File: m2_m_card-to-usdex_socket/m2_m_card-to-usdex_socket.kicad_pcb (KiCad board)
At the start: 6 copper layers, 22 x 80 mm, 11 parts, among them J1 Bus_M.2_Socket_M, J2 Micro_SDex_Card_Det1, U1 AMS1117-1.8

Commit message: m2_m_card-to-usdex_socket: Add impedance information
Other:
- board text added: "Impedance controlled for: JLC06081H-2116 Layers: 6 PCB Thickness: 0.8mm Inner Copper Weight: 0.5oz Outer Copper Weight: 1oz Impedance: 85Ω Type: Differential Pair (Non coplanar) Signal Layer: L1 Top Ref: / Bottom Ref: L2 Trace Spacing: 8 mil Trace Width: 8.0800 mil"
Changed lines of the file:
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@@
+		)
+	)
+	(gr_text "Impedance controlled for: JLC06081H-2116\n\nLayers: 6\nPCB Thickness: 0.8mm\nInner Copper Weight: 0.5oz\nOuter Copper Weight: 1oz\nImpedance: 85Ω\nType: Differential Pair (Non coplanar)\nSignal Layer: L1\nTop Ref: /\nBottom Ref: L2\nTrace Spacing: 8 mil\nTrace Width: 8.0800 mil"
+		(at 220.4 79 0)
+		(layer "Cmts.User")
+		(effects
+			(font
+				(size 1 1)
+				(thickness 0.15)
+			)
+			(justify left bottom)
 		)
 	)

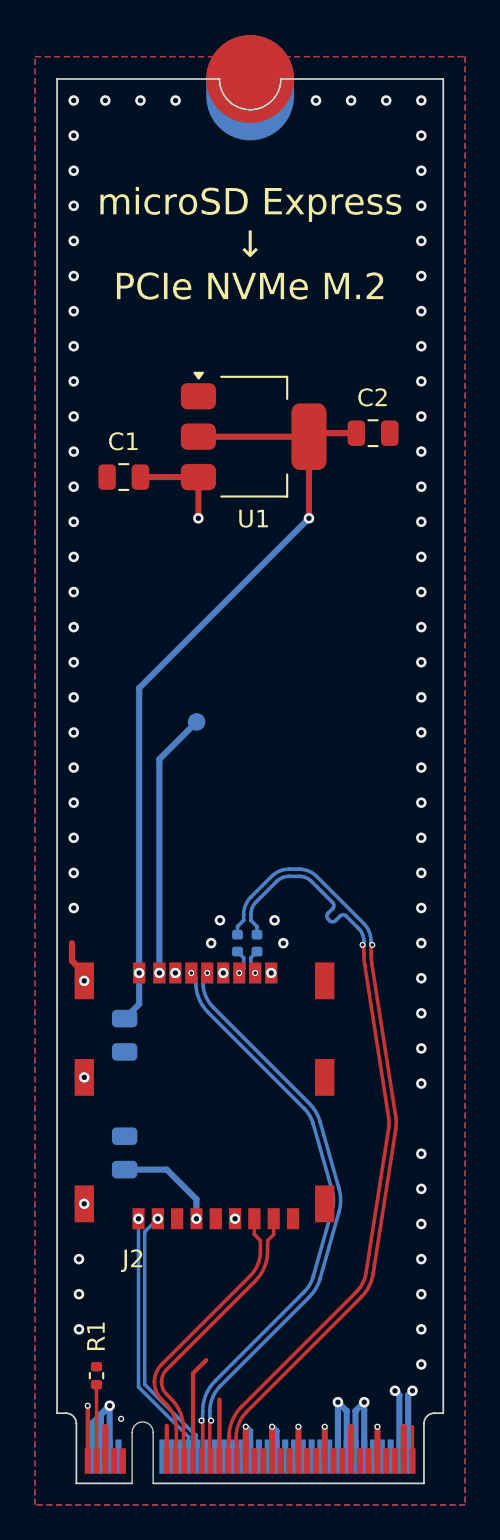
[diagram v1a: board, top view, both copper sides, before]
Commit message: m2_m_card-to-usdex_socket: adjust via holes and smd size
for reduce production cost!
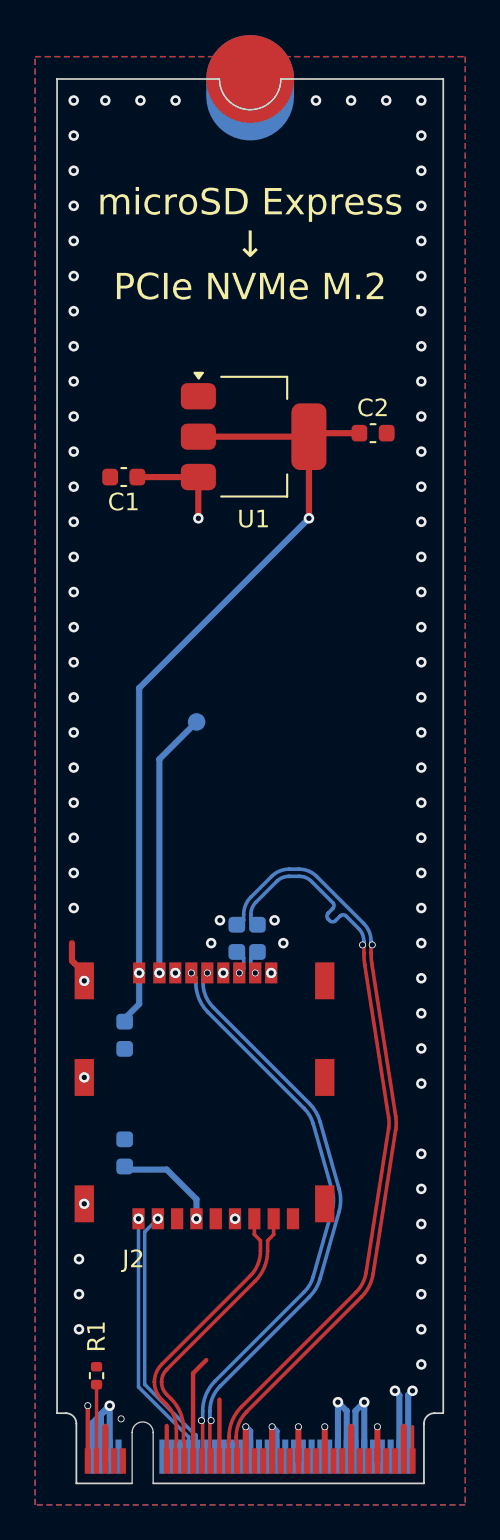
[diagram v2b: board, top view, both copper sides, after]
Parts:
- C1, C2, C3, C6: footprint Capacitor_SMD:C_0805_2012Metric -> Capacitor_SMD:C_0603_1608Metric
- C4, C5: footprint Capacitor_SMD:C_0402_1005Metric -> Capacitor_SMD:C_0603_1608Metric
- moved C4 0.28 mm to (268.5, 105.7)
- moved C5 0.27 mm to (269.7, 105.7)
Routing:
- net PCIe_RX+: track 44.6 -> 43.7 mm
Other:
- board text added: "github.com/m1cha Modified by Choryu"
- board text added: "v1.0-LP"
- board text removed: "github.com/m1cha"
- board text removed: "v1.0"
